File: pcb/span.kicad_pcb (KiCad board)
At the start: 2 copper layers, 232 x 95.3 mm, 94 parts, among them J1 MJ-4PP-9, J2 MJ-4PP-9, J3 OLED, J4 OLED, SW1 SW_PUSH, SW10 SW_PUSH, SW11 SW_PUSH, SW12 SW_PUSH, SW13 SW_PUSH, SW14 SW_PUSH, SW15 SW_PUSH, SW16 SW_PUSH, SW17 SW_PUSH, SW18 SW_PUSH, SW19 SW_PUSH, SW2 SW_PUSH, SW20 SW_PUSH, SW21 SW_PUSH, SW22 SW_PUSH, SW23 SW_PUSH, SW24 SW_PUSH, SW25 SW_PUSH, SW26 SW_PUSH, SW27 SW_PUSH, SW28 SW_PUSH, SW29 SW_PUSH, SW3 SW_PUSH, SW30 SW_PUSH, SW31 SW_PUSH, SW32 SW_PUSH, SW33 SW_PUSH, SW34 SW_PUSH, SW35 SW_PUSH, SW36 SW_PUSH, SW4 SW_PUSH, SW5 SW_PUSH, SW6 SW_PUSH, SW7 SW_PUSH, SW8 SW_PUSH, SW9 SW_PUSH, U1 ProMicro, U2 ProMicro

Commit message: pcb: bump version
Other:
- board text added: "f2f8950"
- board text removed: "731c1e5"

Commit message: pcb: add holykeebs logo, fix attribution
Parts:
- added REF**: logo big, holykeebs:logo .5x, B.Cu at (147.1, 57.3)
- added REF**: logo big, holykeebs:logo .5x, B.Cu at (116.1, 57.2)
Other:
- board text added: "spankbd v1.0 designed by idank"
- board text removed: "spankbd v1.0, designed by idank"

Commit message: pcb: bump version
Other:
- board text added: "ef3f4bf"
- board text removed: "f2f8950"

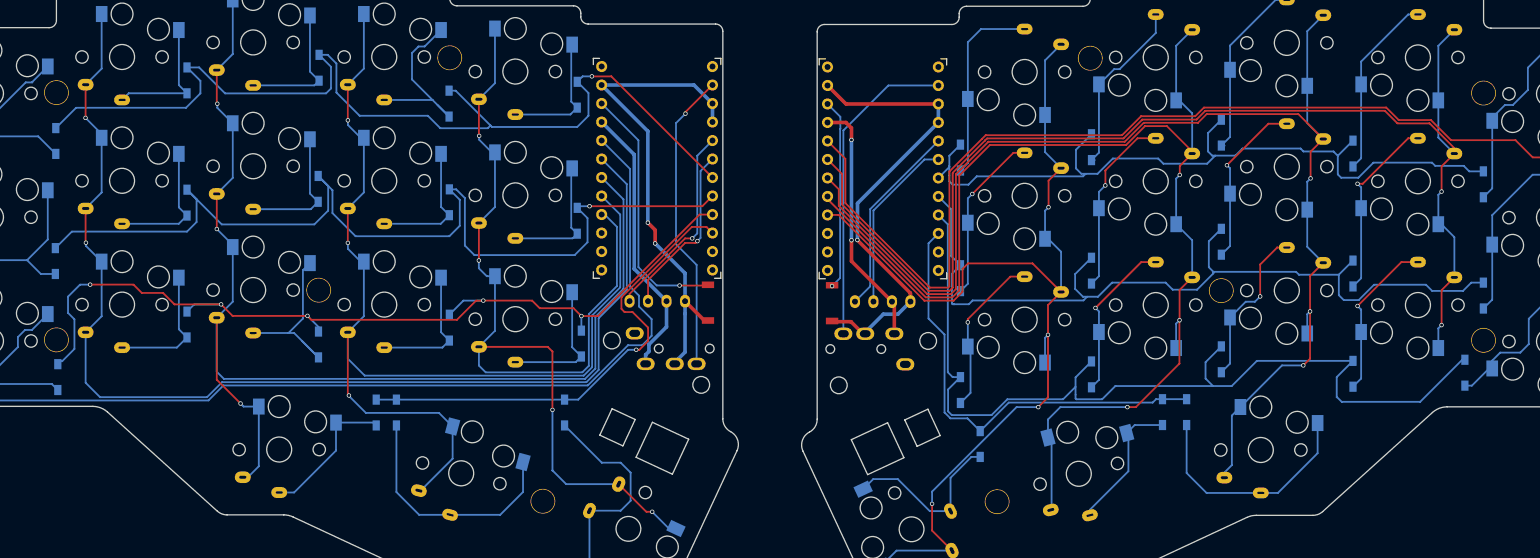
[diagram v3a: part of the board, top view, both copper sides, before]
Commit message: pcb: use slightly bigger holes for the controller pins and  mounting holes
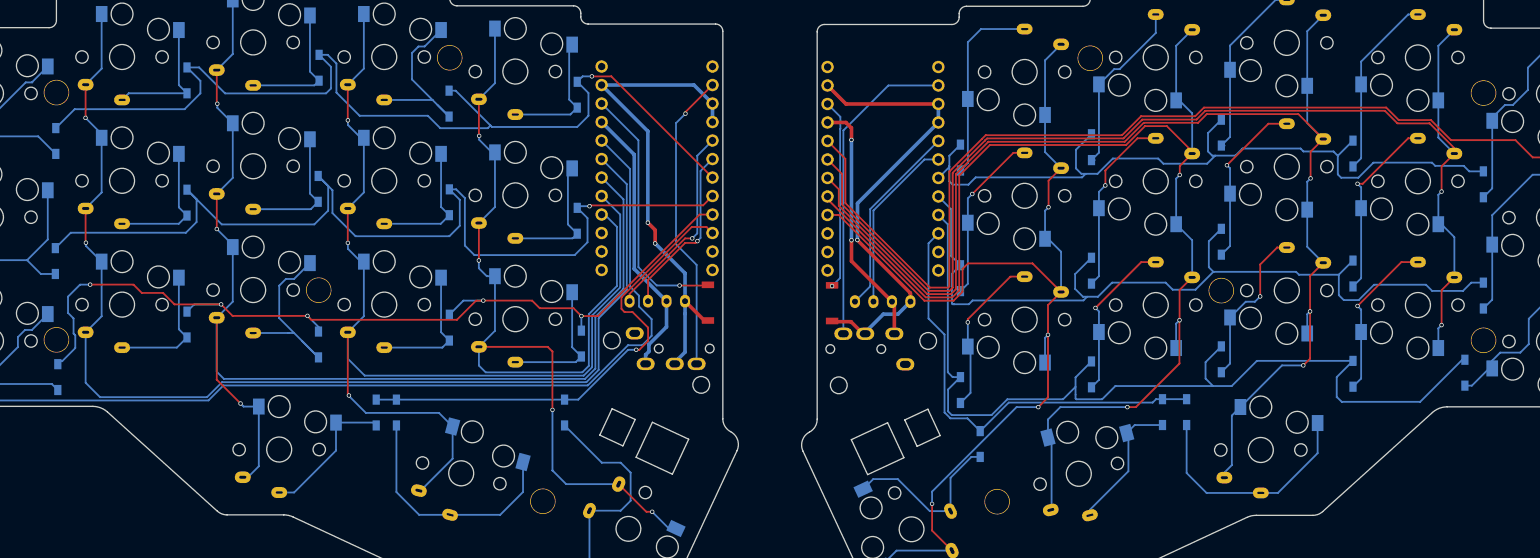
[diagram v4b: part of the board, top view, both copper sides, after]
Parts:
- H1, H10, H2, H3, H4, H5, H6, H7, H8, H9: renamed from REF**; value M2_SPACER -> MountingHole
- U1, U2: footprint kbd:ProMicro_v3 -> holykeebs:ProMicro_1mm_holes
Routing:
- net Net-(D13-A): track 24.4 -> 26.4 mm

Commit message: pcb: bump version
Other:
- board text added: "d74a0ae"
- board text removed: "ef3f4bf"

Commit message: pcb: add filled zones
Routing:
- net Net-(D13-A): track 26.4 -> 23.2 mm
- net Net-(D4-A): track 25.0 -> 22.8 mm
- added copper zone on B.Cu, net (none)
- added copper zone on F.Cu, net (none)

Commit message: pcb: bump version
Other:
- board text added: "a8477fd"
- board text removed: "d74a0ae"
